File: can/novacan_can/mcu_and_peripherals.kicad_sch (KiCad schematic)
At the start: 31 parts, among them J2 ST-LINK, J3 Micro_SD_Card, J4 SERVO_1, J5 SERVO_2, J6 SERVO_3, SW1 SW_Push, U5 STM32F103C8Tx, U6 BME280, U7 MPU-9250, U8 RFM69HCW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

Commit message: added pdf
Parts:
- added J7: UART, symbol Connector:Conn_01x02_Pin
- added SW2: BTN1, symbol Switch:SW_Push
- added SW3: BTN2, symbol Switch:SW_Push
- added SW4: BTN3, symbol Switch:SW_Push
- SW1: value SW_Push -> BTN_RST
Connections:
- net CS_SD: now also U5.22 (PB11); no longer U5.29 (PA8)
- net GND: now also SW2.1, SW3.1, SW4.1
- net BTN_1: now reaches U5.20 (PB2)
- net BTN_1: now also SW2.2, SW3.2, SW4.2
- net USART1_TX: now reaches U5.30 (PA9)
- net USART1_TX: now also J7.1 (Pin_1)
- net USART1_RX: now reaches U5.31 (PA10)
- net USART1_RX: now also J7.2 (Pin_2)
- net BTN_2: now reaches U5.39 (PB3)
- net BTN_3: now reaches U5.40 (PB4)
- no-connect marks 31 -> 26
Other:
- company, title: (none) -> NovaGlider

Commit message: bugfixes + schematic.pdf
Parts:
- removed AE1: Antenna_Shield, symbol Device:Antenna_Shield
- added J8: Conn_Coaxial, Connector_Coaxial:U.FL_Molex_MCRF_73412-0110_Vertical, symbol Connector:Conn_Coaxial
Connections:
- net BTN_1: no longer SW3.2, SW4.2
- net BTN_2: now also SW3.2
- net BTN_3: now also SW4.2
- net GND: now also J8.2 (Ext)
- net I2C1_SCL: now also R11.2; no longer R12.2
- net I2C1_SDA: now also R12.2; no longer R11.2
- net at U8.9 (ANT): now also J8.1 (In)
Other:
- moved on the sheet: C17, C18, C19, J4, J5, J6, R11, R12

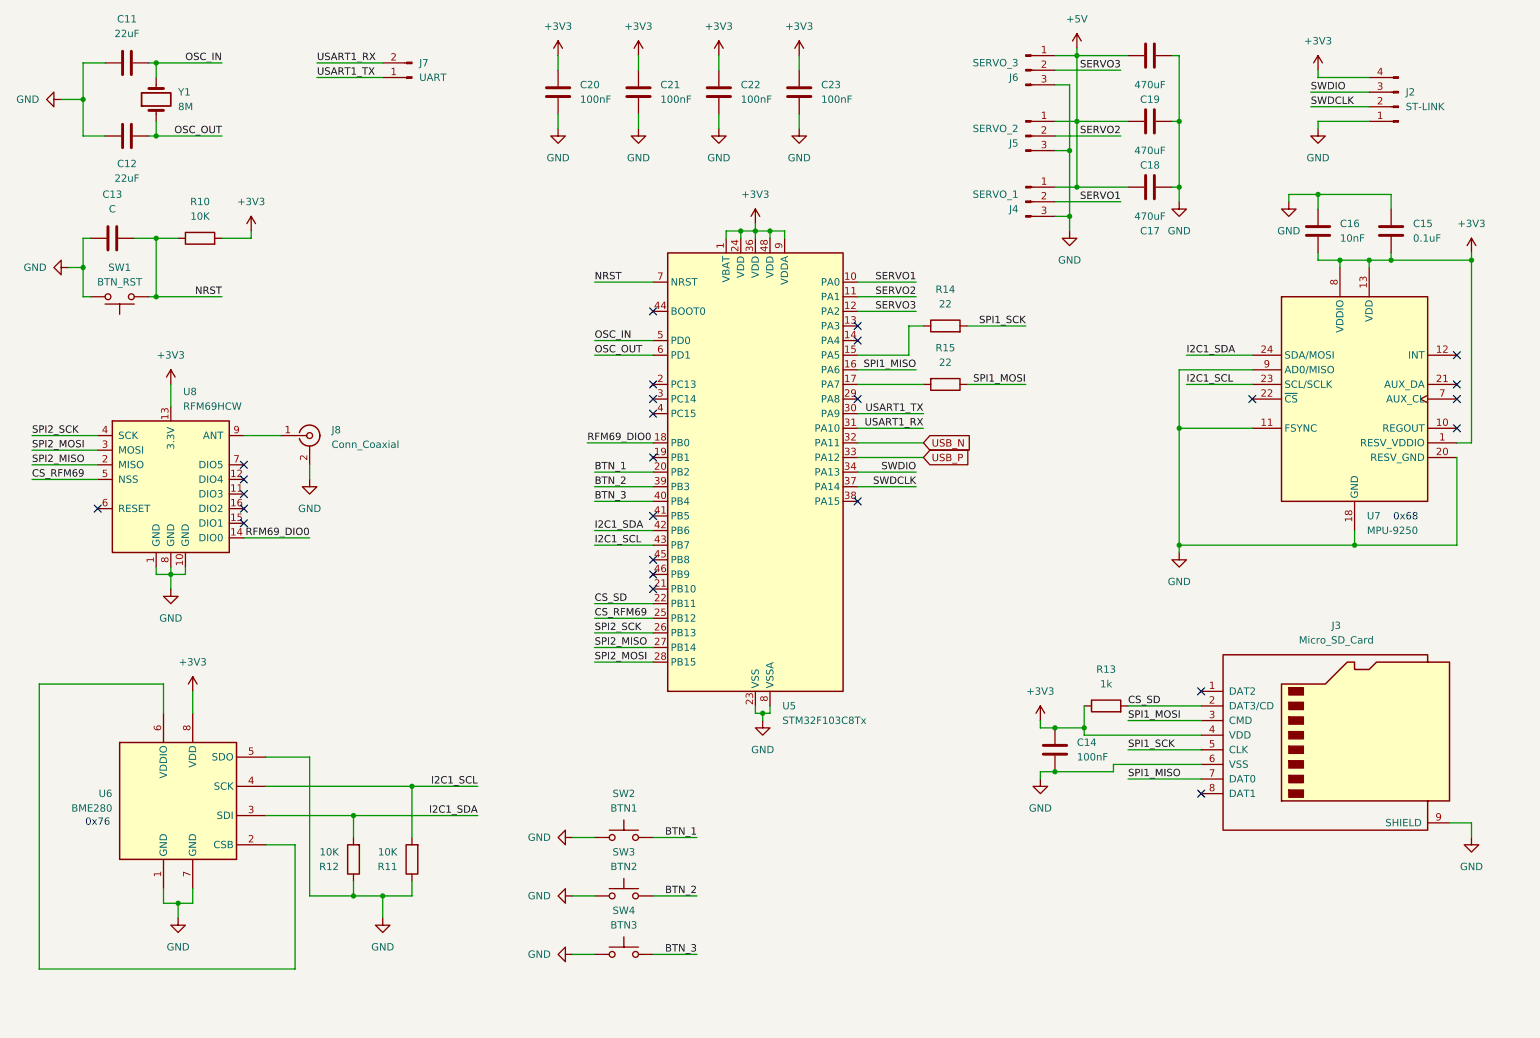
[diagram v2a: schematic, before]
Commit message: added footprints and symbols, changed issues pointed out by reddit users' review
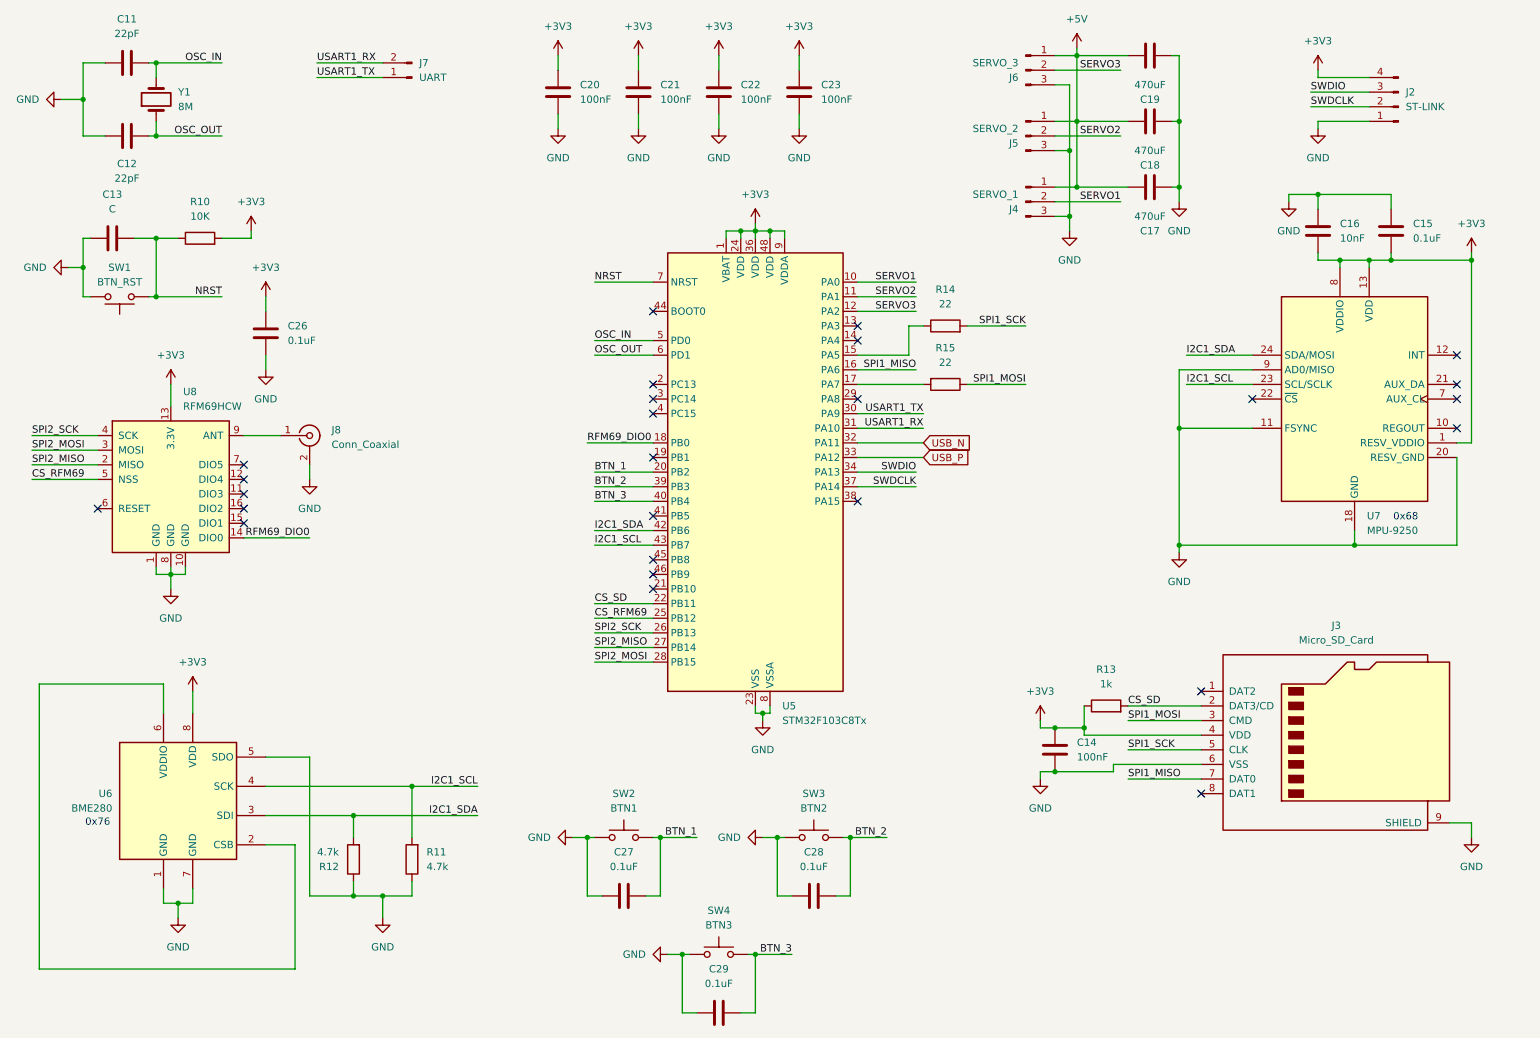
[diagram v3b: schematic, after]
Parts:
- added C26, C27, C28, C29: 0.1uF, symbol Device:C
- C11, C12: value 22uF -> 22pF
- R11, R12: value 10K -> 4.7k
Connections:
- net +3V3: now also C26.1
- net BTN_1: now also C27.2
- net BTN_2: now also C28.2
- net BTN_3: now also C29.2
- net GND: now also C26.2, C27.1, C28.1, C29.1

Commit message: added extra footprints, resolved ESD issues
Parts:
- removed J7: UART, symbol Connector:Conn_01x02_Pin
- added J7: UART, symbol Connector:Conn_01x03_Pin
- added R17, R18: 22, symbol Device:R
- added R19: 1k, symbol Device:R
- added TP1: I2C1_SDA, symbol Connector:TestPoint
- added TP10: SPI1_MOSI, symbol Connector:TestPoint
- added TP11: SPI1_MISO, symbol Connector:TestPoint
- added TP12: CS_SD, symbol Connector:TestPoint
- added TP2: I2C1_SCL, symbol Connector:TestPoint
- added TP3: UART1_TX, symbol Connector:TestPoint
- added TP4: UART1_RX, symbol Connector:TestPoint
- added TP5: CS_RFM69, symbol Connector:TestPoint
- added TP6: SPI2_SCK, symbol Connector:TestPoint
- added TP7: SPI2_MISO, symbol Connector:TestPoint
- added TP8: SPI2_MOSI, symbol Connector:TestPoint
- added TP9: SPI1_SCK, symbol Connector:TestPoint
- R10: value 10K -> 10k
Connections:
- net +3V3: now also R19.2
- net CS_RFM69: now also R19.1, TP5.1
- net CS_SD: now also TP12.1
- net GND: now also J7.1 (Pin_1)
- net I2C1_SCL: now also TP2.1
- net I2C1_SDA: now also TP1.1
- net SPI1_MISO: now also TP11.1
- net SPI1_MOSI: now also TP10.1
- net SPI1_SCK: now also TP9.1
- net SPI2_MISO: now also TP7.1
- net SPI2_MOSI: now also R18.1, TP8.1; no longer U5.28 (PB15)
- net SPI2_SCK: now also R17.1, TP6.1; no longer U5.26 (PB13)
- net USART1_RX: now also J7.3 (Pin_3), TP4.1
- net USART1_TX: now also J7.2 (Pin_2), TP3.1
- net RES_RFM69: now reaches U8.6 (RESET)
- net RES_RFM69: now also U5.19 (PB1)
- new net: R17.2, U5.26 (PB13)
- new net: R18.2, U5.28 (PB15)
- no-connect marks 26 -> 24
